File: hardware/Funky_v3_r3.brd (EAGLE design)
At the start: 21.8 x 22.6 mm, 43 parts, among them IC2 LTC3525, IC3 MCP1703CB, Q1 P-MOSFET, U3 ATMEGA32U4, Y1 8MHz

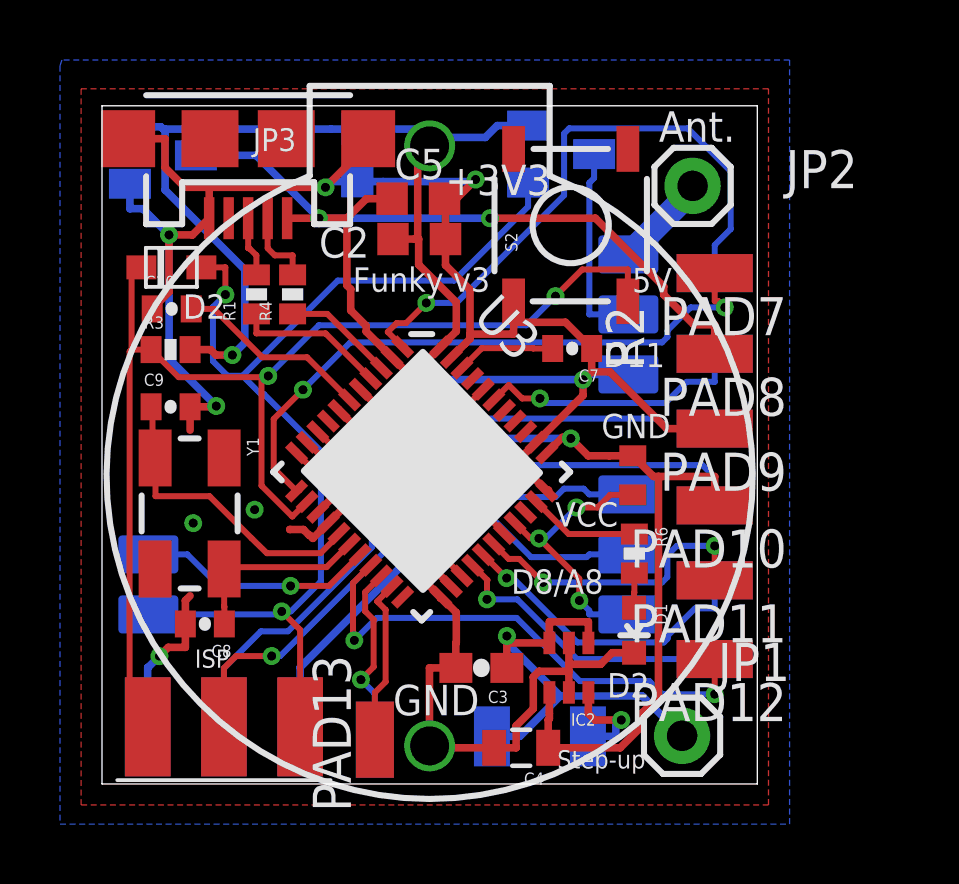
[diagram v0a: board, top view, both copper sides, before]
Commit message: Hardware update
Node 1.0.0, export and node shield
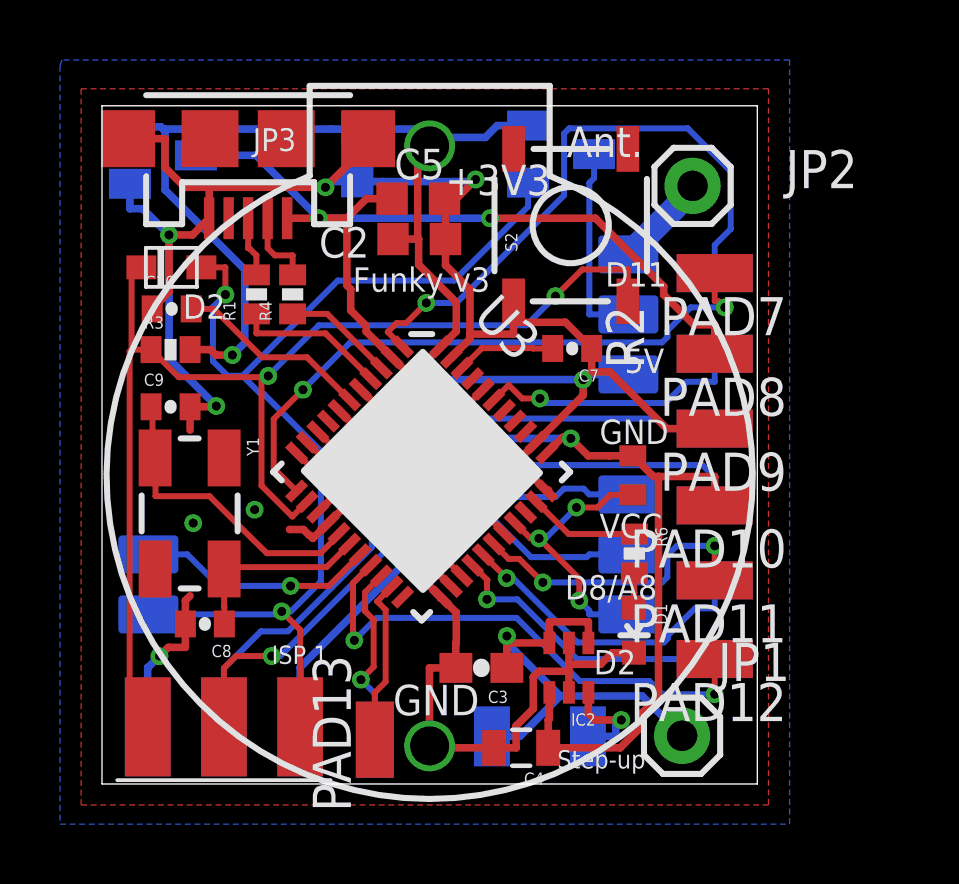
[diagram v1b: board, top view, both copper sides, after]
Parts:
- renumbered IC3 to TOREX-XC6206
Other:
- board text added: "ISP 1"
- board text removed: "ISP"
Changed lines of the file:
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@@
 <?xml version="1.0" encoding="utf-8"?>
 <!DOCTYPE eagle SYSTEM "eagle.dtd">
-<eagle version="6.5.0">
+<eagle version="6.1">
 <drawing>
 <settings>
@@
 <wire x1="3.81" y1="3.937" x2="3.81" y2="0.889" width="0.4064" layer="42"/>
 <wire x1="6.35" y1="3.937" x2="6.35" y2="0.889" width="0.4064" layer="42"/>
-<text x="4.109" y="4.382" size="0.6096" layer="21">ISP</text>
+<text x="6.669" y="4.51" size="0.6096" layer="21">ISP 1</text>
 <text x="13.594" y="3.813" size="1.016" layer="21" rot="R180">GND</text>
 <text x="12.462" y="20.134" size="1.016" layer="21">+3V3</text>
-<text x="19.577" y="21.914" size="1.016" layer="21">Ant.</text>
-<text x="18.688" y="16.896" size="0.8128" layer="21" font="vector">5V</text>
-<text x="17.728" y="14.4" size="0.8128" layer="21" font="vector">D11</text>
-<text x="17.664" y="12.032" size="0.8128" layer="21" font="vector">GND</text>
-<text x="16.128" y="9.088" size="0.8128" layer="21" font="vector">VCC</text>
-<text x="14.656" y="6.848" size="0.8128" layer="21" font="vector">D8/A8</text>
-<text x="17.856" y="3.392" size="0.8128" layer="21" font="vector">D2</text>
+<text x="16.505" y="21.402" size="1.016" layer="21">Ant.</text>
+<text x="18.432" y="14.208" size="0.8128" layer="21" font="vector">5V</text>
+<text x="17.792" y="17.088" size="0.8128" layer="21" font="vector">D11</text>
+<text x="17.6" y="11.84" size="0.8128" layer="21" font="vector">GND</text>
+<text x="17.6" y="8.704" size="0.8128" layer="21" font="vector">VCC</text>
+<text x="16.448" y="6.656" size="0.8128" layer="21" font="vector">D8/A8</text>
+<text x="17.408" y="4.16" size="0.8128" layer="21" font="vector">D2</text>
 <text x="16.192" y="1.024" size="0.6096" layer="21" font="vector">Step-up</text>
 <text x="13.952" y="17.728" size="0.8128" layer="21" font="vector" rot="R180">Funky v3</text>
@@
 </class>
 </classes>
-<designrules name="default">
+<designrules>
 <description language="de">&lt;b&gt;EAGLE Design Rules Prototypen  für PCB-POOL(R)&lt;/b&gt;
 &lt;p&gt;
@@
 <element name="IC2" library="JeeLabs" package="SC70" value="LTC3525" x="16.579" y="4.384" rot="R180"/>
 <element name="L1" library="SparkFun" package="1210" value="10 µH" x="15.614" y="2.095" rot="MR180"/>
-<element name="IC3" library="linear" package="SOT23" value="MCP1703CB" x="3.048" y="21.463" rot="MR90"/>
+<element name="TOREX-XC6206" library="linear" package="SOT23" value="MCP1703CB" x="3.048" y="21.463" rot="MR90"/>
 <element name="C5" library="rcl" package="C0603K" value="1uF" x="11.56" y="20.016"/>
 <element name="C6" library="rcl" package="C0603K" value="1u" x="9.525" y="21.463" rot="MR270"/>
@@
 <contactref element="C6" pad="1"/>
 <contactref element="PAD10" pad="1"/>
-<contactref element="IC3" pad="2"/>
+<contactref element="TOREX-XC6206" pad="2"/>
 <wire x1="12.3169" y1="12.1841" x2="12.476" y2="12.025" width="0.254" layer="16"/>
 <wire x1="12.476" y1="12.025" x2="16.6437" y2="12.025" width="0.254" layer="16"/>
@@
 <contactref element="C6" pad="2"/>
 <contactref element="C5" pad="2"/>
-<contactref element="IC3" pad="1"/>
+<contactref element="TOREX-XC6206" pad="1"/>
 <contactref element="C7" pad="1"/>
 <contactref element="C8" pad="2"/>
@@
 </signal>
 <signal name="VBUS" class="1">
-<contactref element="IC3" pad="3"/>
+<contactref element="TOREX-XC6206" pad="3"/>
 <contactref element="C5" pad="1"/>
 <contactref element="U3" pad="7"/>
